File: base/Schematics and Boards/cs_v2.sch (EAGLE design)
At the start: 22 parts, among them U1 ATSAMD51, Y1 TSX-3225_16.0000MF09Z-AC3

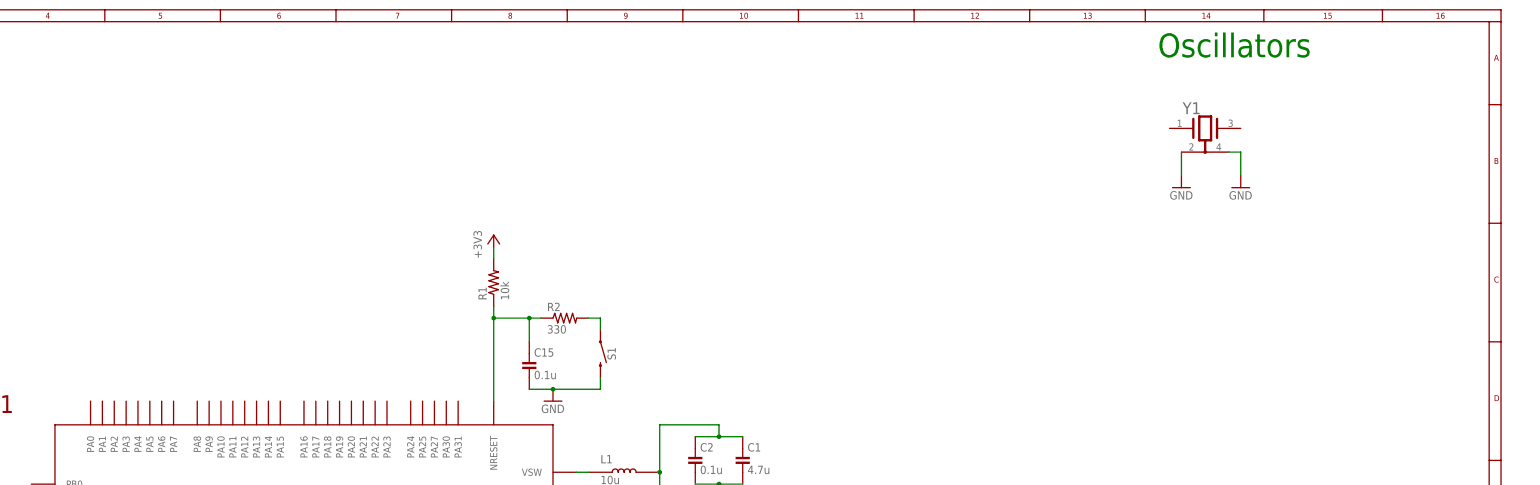
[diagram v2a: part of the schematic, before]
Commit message: Add crystals with loads and part numbers
16 MHz fast osc and 32.768 slow.
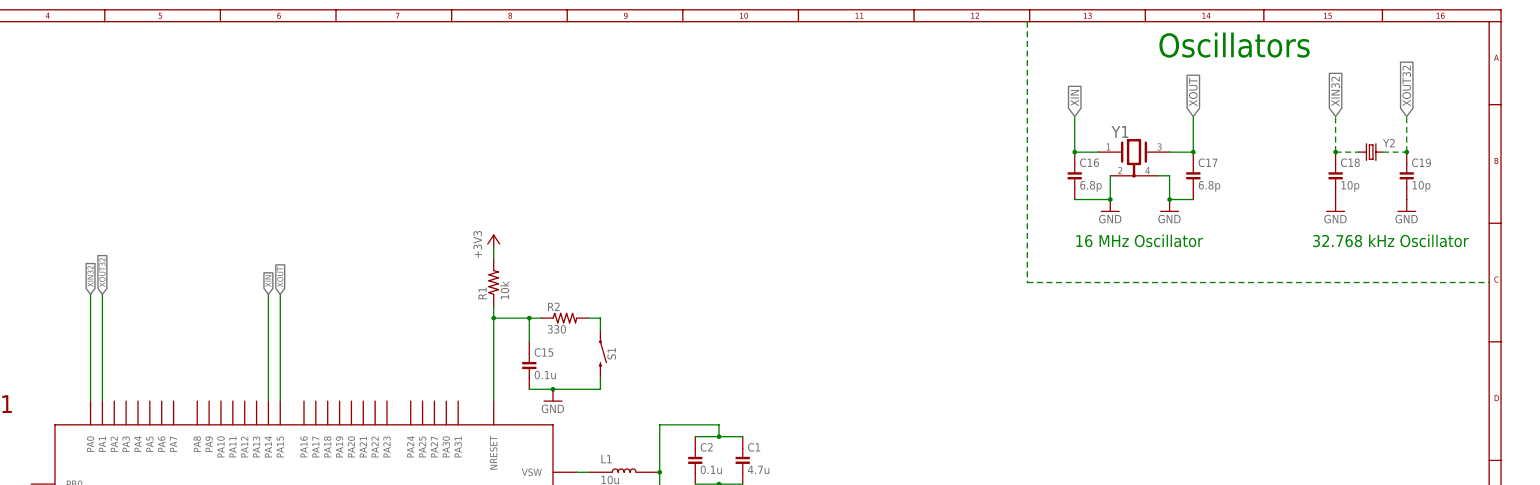
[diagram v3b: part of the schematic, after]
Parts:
- added C16, C17: 6.8p, Capacitors:C-0402
- added C18, C19: 10p, Capacitors:C-0402
- added Y2: ABRACON_ABS07-32.768KHZ-9-TABRACON_ABS07-32.768KHZ-7-T_0_0, Oscillators:ABRACON_ABS07-32.768KHZ-9-TABRACON_ABS07-32.768KHZ-7-T_0_0
- Y1: value TSX-3225_16.0000MF09Z-AC3 -> 16M
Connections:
- new net XIN: C16.1, U1.PA14, Y1.1
- new net XIN32: C18.1, U1.PA0, Y2.1
- new net XOUT: C17.1, U1.PA15, Y1.3
- new net XOUT32: C19.1, U1.PA1, Y2.2
- net GND: now also C16.2, C17.2, C18.2, C19.2
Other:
- note added: "16 MHz Oscillator"
- note added: "32.768 kHz Oscillator"
- moved on the sheet: Y1
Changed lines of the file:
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@@
 </part>
 <part name="S1" library="SparkFun-Switches" deviceset="MOMENTARY-SWITCH-SPST" device="-SMD-4.6X2.8MM"/>
-<part name="Y1" library="Oscillators" deviceset="TSX-3225_16.0000MF09Z-AC3" device=""/>
+<part name="Y1" library="Oscillators" deviceset="TSX-3225_16.0000MF09Z-AC3" device="" value="16M"/>
 <part name="GND6" library="Supplies" deviceset="GND" device=""/>
 <part name="GND8" library="Supplies" deviceset="GND" device=""/>
+<part name="C16" library="Capacitors" deviceset="C-" device="0402" value="6.8p">
+<attribute name="PART_NO" value="C0402C689D8GAC7867"/>
+</part>
+<part name="C17" library="Capacitors" deviceset="C-" device="0402" value="6.8p">
+<attribute name="PART_NO" value="C0402C689D8GAC7867"/>
+</part>
+<part name="Y2" library="Oscillators" deviceset="ABRACON_ABS07-32.768KHZ-9-T" device="ABRACON_ABS07-32.768KHZ-7-T_0_0"/>
+<part name="C18" library="Capacitors" deviceset="C-" device="0402" value="10p">
+<attribute name="PART_NO" value="C0402C100C8GACTU"/>
+</part>
+<part name="C19" library="Capacitors" deviceset="C-" device="0402" value="10p">
+<attribute name="PART_NO" value="C0402C100C8GACTU"/>
+</part>
+<part name="GND9" library="Supplies" deviceset="GND" device=""/>
+<part name="GND10" library="Supplies" deviceset="GND" device=""/>
 </parts>
 <sheets>
@@
 <text x="228.6" y="162.56" size="1.778" layer="91">Sch Checklist fig 59-1</text>
 <text x="325.12" y="264.16" size="5.08" layer="91">Oscillators</text>
+<text x="307.34" y="223.52" size="2.54" layer="91">16 MHz Oscillator</text>
+<text x="358.14" y="223.52" size="2.54" layer="91">32.768 kHz Oscillator</text>
 </plain>
 <instances>
@@
 <attribute name="NAME" x="207.264" y="200.66" size="1.778" layer="95" font="vector" rot="R270" align="bottom-center"/>
 </instance>
-<instance part="Y1" gate="A" x="330.2" y="256.54" smashed="yes">
-<attribute name="NAME" x="330.454" y="254.508" size="2.54" layer="95" align="top-left"/>
-</instance>
-<instance part="GND6" gate="1" x="330.2" y="236.22" smashed="yes">
-<attribute name="VALUE" x="327.66" y="233.68" size="1.778" layer="96"/>
-</instance>
-<instance part="GND8" gate="1" x="342.9" y="236.22" smashed="yes">
-<attribute name="VALUE" x="340.36" y="233.68" size="1.778" layer="96"/>
+<instance part="Y1" gate="A" x="314.96" y="251.46" smashed="yes">
+<attribute name="NAME" x="315.214" y="249.428" size="2.54" layer="95" align="top-left"/>
+</instance>
+<instance part="GND6" gate="1" x="314.96" y="231.14" smashed="yes">
+<attribute name="VALUE" x="312.42" y="228.6" size="1.778" layer="96"/>
+</instance>
+<instance part="GND8" gate="1" x="327.66" y="231.14" smashed="yes">
+<attribute name="VALUE" x="325.12" y="228.6" size="1.778" layer="96"/>
+</instance>
+<instance part="C16" gate="G$1" x="307.34" y="238.76" smashed="yes">
+<attribute name="NAME" x="308.356" y="240.665" size="1.778" layer="95"/>
+<attribute name="VALUE" x="308.356" y="235.839" size="1.778" layer="96"/>
+<attribute name="PART_NO" x="307.34" y="238.76" size="2.54" layer="96" display="off"/>
+</instance>
+<instance part="C17" gate="G$1" x="332.74" y="238.76" smashed="yes">
+<attribute name="NAME" x="333.756" y="240.665" size="1.778" layer="95"/>
+<attribute name="VALUE" x="333.756" y="235.839" size="1.778" layer="96"/>
+<attribute name="PART_NO" x="332.74" y="238.76" size="2.54" layer="96" display="off"/>
+</instance>
+<instance part="Y2" gate="G$1" x="370.84" y="243.84" smashed="yes">
+<attribute name="NAME" x="373.38" y="244.856" size="1.778" layer="95"/>
+</instance>
+<instance part="C18" gate="G$1" x="363.22" y="238.76" smashed="yes">
+<attribute name="NAME" x="364.236" y="240.665" size="1.778" layer="95"/>
+<attribute name="VALUE" x="364.236" y="235.839" size="1.778" layer="96"/>
+<attribute name="PART_NO" x="363.22" y="238.76" size="2.54" layer="96" display="off"/>
+</instance>
+<instance part="C19" gate="G$1" x="378.46" y="238.76" smashed="yes">
+<attribute name="NAME" x="379.476" y="240.665" size="1.778" layer="95"/>
+<attribute name="VALUE" x="379.476" y="235.839" size="1.778" layer="96"/>
+<attribute name="PART_NO" x="378.46" y="238.76" size="2.54" layer="96" display="off"/>
+</instance>
+<instance part="GND9" gate="1" x="363.22" y="231.14" smashed="yes">
+<attribute name="VALUE" x="360.68" y="228.6" size="1.778" layer="96"/>
+</instance>
+<instance part="GND10" gate="1" x="378.46" y="231.14" smashed="yes">
+<attribute name="VALUE" x="375.92" y="228.6" size="1.778" layer="96"/>
 </instance>
 </instances>
@@
 <segment>
 <pinref part="GND6" gate="1" pin="GND"/>
-<wire x1="330.2" y1="238.76" x2="330.2" y2="243.84" width="0.1524" layer="91"/>
+<wire x1="314.96" y1="233.68" x2="314.96" y2="238.76" width="0.1524" layer="91"/>
 <pinref part="Y1" gate="A" pin="1_GND"/>
+<pinref part="C16" gate="G$1" pin="2"/>
+<wire x1="307.34" y1="233.68" x2="314.96" y2="233.68" width="0.1524" layer="91"/>
+<junction x="314.96" y="233.68"/>
 </segment>
 <segment>
 <pinref part="GND8" gate="1" pin="GND"/>
 <pinref part="Y1" gate="A" pin="2_GND"/>
-<wire x1="342.9" y1="238.76" x2="342.9" y2="243.84" width="0.1524" layer="91"/>
-<wire x1="342.9" y1="243.84" x2="340.36" y2="243.84" width="0.1524" layer="91"/>
+<wire x1="327.66" y1="233.68" x2="327.66" y2="238.76" width="0.1524" layer="91"/>
+<wire x1="327.66" y1="238.76" x2="325.12" y2="238.76" width="0.1524" layer="91"/>
+<pinref part="C17" gate="G$1" pin="2"/>
+<wire x1="327.66" y1="233.68" x2="332.74" y2="233.68" width="0.1524" layer="91"/>
+<junction x="327.66" y="233.68"/>
+</segment>
+<segment>
+<pinref part="C18" gate="G$1" pin="2"/>
+<pinref part="GND9" gate="1" pin="GND"/>
+</segment>
+<segment>
+<pinref part="C19" gate="G$1" pin="2"/>
+<pinref part="GND10" gate="1" pin="GND"/>
 </segment>
 </net>
@@
 </segment>
 </net>
+<net name="XOUT" class="0">
+<segment>
+<pinref part="C17" gate="G$1" pin="1"/>
+<pinref part="Y1" gate="A" pin="3"/>
+<wire x1="332.74" y1="243.84" x2="327.66" y2="243.84" width="0.1524" layer="91"/>
+<wire x1="332.74" y1="243.84" x2="332.74" y2="251.46" width="0.1524" layer="91"/>
+<junction x="332.74" y="243.84"/>
+<label x="332.74" y="251.46" size="1.778" layer="95" rot="R90" xref="yes"/>
+</segment>
+<segment>
+<pinref part="U1" gate="G$1" pin="PA15"/>
+<wire x1="137.16" y1="190.5" x2="137.16" y2="213.36" width="0.1524" layer="91"/>
+<label x="137.16" y="213.36" size="1.27" layer="95" rot="R90" xref="yes"/>
+</segment>
+</net>
+<net name="XIN" class="0">
+<segment>
+<pinref part="C16" gate="G$1" pin="1"/>
+<pinref part="Y1" gate="A" pin="1"/>
+<wire x1="307.34" y1="243.84" x2="312.42" y2="243.84" width="0.1524" layer="91"/>
+<wire x1="307.34" y1="243.84" x2="307.34" y2="251.46" width="0.1524" layer="91"/>
+<junction x="307.34" y="243.84"/>
+<label x="307.34" y="251.46" size="1.778" layer="95" rot="R90" xref="yes"/>
+</segment>
+<segment>
+<pinref part="U1" gate="G$1" pin="PA14"/>
+<wire x1="134.62" y1="190.5" x2="134.62" y2="213.36" width="0.1524" layer="91"/>
+<label x="134.62" y="213.36" size="1.27" layer="95" rot="R90" xref="yes"/>
+</segment>
+</net>
+<net name="N$4" class="0">
+<segment>
+<wire x1="297.18" y1="271.78" x2="297.18" y2="215.9" width="0.254" layer="91" style="shortdash"/>
+<wire x1="297.18" y1="215.9" x2="396.24" y2="215.9" width="0.254" layer="91" style="shortdash"/>
+</segment>
+</net>
+<net name="XIN32" class="0">
+<segment>
+<pinref part="C18" gate="G$1" pin="1"/>
+<pinref part="Y2" gate="G$1" pin="1"/>
+<wire x1="363.22" y1="243.84" x2="368.3" y2="243.84" width="0.1524" layer="91" style="longdash"/>
+<wire x1="363.22" y1="243.84" x2="363.22" y2="251.46" width="0.1524" layer="91" style="longdash"/>
+<junction x="363.22" y="243.84"/>
+<label x="363.22" y="251.46" size="1.778" layer="95" rot="R90" xref="yes"/>
+</segment>
+<segment>
+<pinref part="U1" gate="G$1" pin="PA0"/>
+<wire x1="96.52" y1="213.36" x2="96.52" y2="190.5" width="0.1524" layer="91"/>
+<label x="96.52" y="213.36" size="1.27" layer="95" rot="R90" xref="yes"/>
+</segment>
+</net>
+<net name="XOUT32" class="0">
+<segment>
+<pinref part="Y2" gate="G$1" pin="2"/>
+<pinref part="C19" gate="G$1" pin="1"/>
+<wire x1="373.38" y1="243.84" x2="378.46" y2="243.84" width="0.1524" layer="91" style="longdash"/>
+<wire x1="378.46" y1="243.84" x2="378.46" y2="251.46" width="0.1524" layer="91" style="longdash"/>
+<junction x="378.46" y="243.84"/>
+<label x="378.46" y="251.46" size="1.778" layer="95" rot="R90" xref="yes"/>
+</segment>
+<segment>
+<pinref part="U1" gate="G$1" pin="PA1"/>
+<wire x1="99.06" y1="190.5" x2="99.06" y2="213.36" width="0.1524" layer="91"/>
+<label x="99.06" y="213.36" size="1.27" layer="95" rot="R90" xref="yes"/>
+</segment>
+</net>

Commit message: Add SD card parts, start on power subsystem
SD card parts added, but not connected to processor. Began on power subsystem. Decided to go with buck boost convertor from maxim. A few TI parts seemed like decent alternatives because they actually post their low-current efficiencies. Would be smart to inquire with maxim.
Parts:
- added C202: 100n, Capacitors:C-0402
- added C206: 470n, Capacitors:C-0402
- added J1: DM3AT-SF-PEJM5, DM3AT-SF-PEJM5:DM3AT-SF-PEJM5
- added J2: (no value), Connectors:J-JST2-SMT_RA-SH
- added R_SDCMD: 10K, Resistors:R-0402
- added R_SD_DET1: 510k, Resistors:R-0402
- added S2: (no value), Switches:SLIDESWITCH-SPDT-SMD-RIGHT-ANGLE
- added U2: MAX77827BEWC+T, Regulators:MAX77827BEWC+T
- added U202: COULOMB-MAX17262, CoulombCounters:COULOMB-MAX17262
- Y1: device Oscillators:TSX-3225_16.0000MF09Z-AC3 -> Oscillators:EPSON_TSX-3225_16.0000MF09Z-AC3
- Y2: value ABRACON_ABS07-32.768KHZ-9-TABRACON_ABS07-32.768KHZ-7-T_0_0 -> ABS07-32.768KHZ-9-T; device Oscillators:ABRACON_ABS07-32.768KHZ-9-TABRACON_ABS07-32.768KHZ-7-T_0_0 -> Oscillators:ABS07-32.768KHZ-9-T
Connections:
- net +3V3 renamed +3V3_PROC
- removed net GND1: C11.2, C12.2, C13.2
- new net +3V3_SD: J1.VDD, R_SDCMD.2, R_SD_DET1.1
- new net +3V7_BATT: U202.SYS
- new net +3V7_BATT_IN: C202.1, S2.S, U202.BATT, U202.TH
- new net ADDR_I2C_CLK: U202.SCL
- new net ADDR_I2C_DAT: U202.SDA
- new net BATT_ALERT: U202.ALRT
- new net N$13: C206.1, U202.REG
- new net N$7: J2.1, S2.P
- new net N$8: S2.O
- new net SDIO_CLK: J1.CLK
- new net SDIO_CMD: J1.CMD, R_SDCMD.1
- new net SDIO_D0: J1.DAT0
- new net SDIO_D1: J1.DAT1
- new net SDIO_D2: J1.DAT2
- new net SDIO_D3: J1.CD/DAT3
- new net SD_DETECT: J1.A, R_SD_DET1.2
- net GND: now also C11.2, C12.2, C13.2, C202.2, C206.2, J1.B, J1.SHIELD, J1.VSS, J2.2, U202.GND
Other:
- note added: "3V7 BATT needs to be included in the debug header so that it can charge the battery from there; no charger on this board"
- note added: "Double check polarity!!"
- note added: "Using SH type connector (1mm pitch), as opposed to PH type (2mm pitch). Height chopped in half, but carries less current (1A rating) and is more prone to rip off. Unlikely to find many batteries with this connector by default."
- note removed: "Separate analog GND?"

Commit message: Add load switch, sense resistors, breakout headers, and comments
Load switch for SD card.

Sense resistors daughter card header, processor, and SD card.

Added 80 and 30 pin receptacles to design for daughter and debug cards, respectively. Pin count is a guess for now.

Comments for power subsystem. In particular, comments on sense resistors and charging circuit (residing on debug card).
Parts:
- added C20: 0.1u, Capacitors:C-0402
- added C21: 1u, Capacitors:C-0603
- added C_REG_BIAS: 1u, Capacitors:C-0402
- added C_REG_IN: 10u, Capacitors:C-0603
- added C_REG_OUT: 22u, Capacitors:C-0805
- added J_DBG: HIROSE_DF40_30-PIN_CONNECTORS, Connectors:HIROSE_DF40_30-PIN_CONNECTORS
- added J_DTR: HIROSE-DF40_80-PIN_CONNECTORS, Connectors:HIROSE-DF40_80-PIN_CONNECTORS
- added L3: 1u, Inductors:L1008
- added R3: 0, Resistors:R-2010
- added R_SENSE_DTR: 0.5, Resistors:R-0603
- added R_SENSE_PROC, R_SENSE_SD: 1, Resistors:R-0603
- added U206: LOADSWITCH-MIC94162, Switches:LOADSWITCH-MIC94162
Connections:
- new net +3V3: C_REG_OUT.1, R_SENSE_DTR.1, R_SENSE_PROC.1, R_SENSE_SD.1, U2.OUT, U2.OUTS
- new net +3V3_DTR: R_SENSE_DTR.2
- new net +3V3_SD_SENSE: C21.1, R_SENSE_SD.2, U206.VIN
- new net AGND: C_REG_BIAS.2, R3.1, U2.AGND
- new net EN_SD: U206.ENABLE
- new net N$10: L3.2, U2.LX2
- new net N$11: C_REG_BIAS.1, U2.BIAS
- new net N$9: L3.1, U2.LX1
- net +3V3_PROC: now also R_SENSE_PROC.2
- net +3V3_SD: now also C20.1, U206.VOUT
- net +3V7_BATT: now also C_REG_IN.1, U2.EN, U2.IN
- net GND: now also C20.2, C21.2, C_REG_IN.2, C_REG_OUT.2, R3.2, U2.FPWM, U2.PGND, U206.GND
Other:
- note added: "Need p-channel mosfet here to select between battery input and the charger output from debug. Switch enabled by that votlage from charger"
- note added: "POK is open drain output. Unused, so left floating. SEL left open for 3V3 output. Both SEL and POK are center pins in WLP, so simplest to leave unused or tied to GND"
- note added: "Pinout Headers"
- note added: "Power"
- note added: "Processor"
- note added: "Route analog signals through this resistor. The resistor is big and fat for this purpose!"
- note added: "Sense resistor values are suggetions. These values may need to be updated. They should, for max current draw, have no more than 100 mV drop on 3.3V output."
- note added: "Sense resistors exist for high side current monitors. Another processor/ADC on the debug board should calculate the differential voltage across the resistor, and use this to determine power input to the load at high resolution. Differential voltage should be at most 100 mV, so an amplifier should scale up that differential voltage"

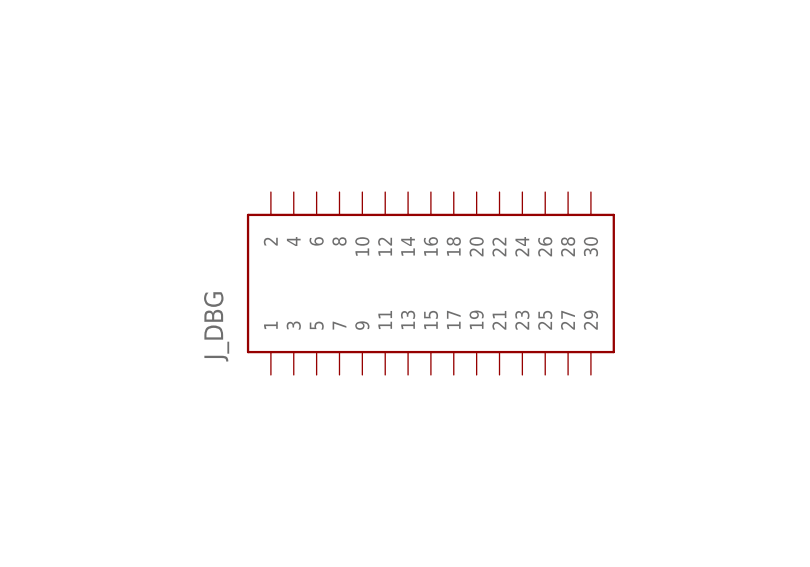
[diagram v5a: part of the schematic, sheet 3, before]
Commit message: Remove 30-pin header temporarily -- bad footprint
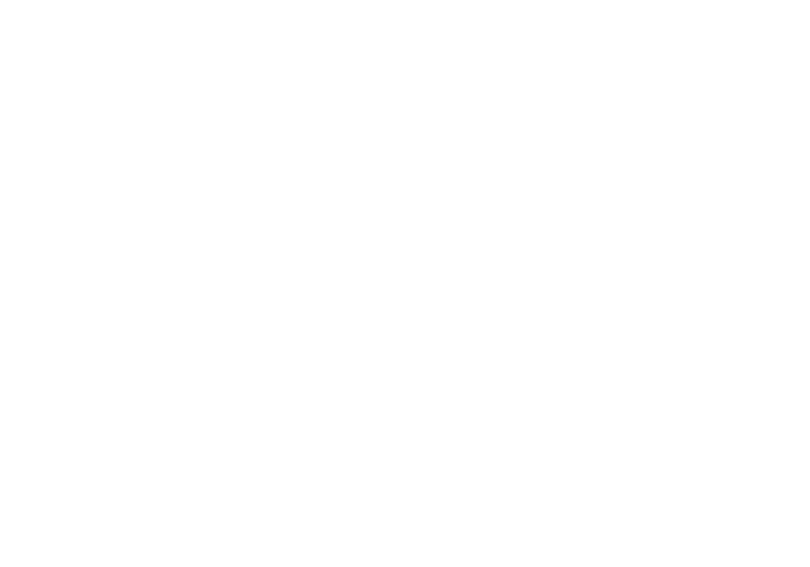
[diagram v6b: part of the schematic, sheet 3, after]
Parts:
- removed J_DBG: HIROSE_DF40_30-PIN_CONNECTORS, Connectors:HIROSE_DF40_30-PIN_CONNECTORS
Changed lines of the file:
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@@
 </part>
 <part name="BORDER4" library="Graphics" deviceset="BORDER-CMU" device=""/>
-<part name="J_DBG" library="Connectors" deviceset="HIROSE_DF40_30-PIN_CONNECTORS" device=""/>
 <part name="J_DTR" library="Connectors" deviceset="HIROSE-DF40_80-PIN_CONNECTORS" device=""/>
 </parts>
@@
 <attribute name="SHEET" x="337.82" y="4.2672" size="1.778" layer="94"/>
 </instance>
-<instance part="J_DBG" gate="A" x="294.64" y="137.16" smashed="yes" rot="R90">
-<attribute name="NAME" x="289.3314" y="141.3256" size="2.0828" layer="95" ratio="6" rot="SR90"/>
-</instance>
 <instance part="J_DTR" gate="G$1" x="132.08" y="149.86" smashed="yes" rot="R90">

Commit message: Add power source selection; clean up pwr subsystem
Battery charger will not be on main board, so power source selection hardware needs to be here to provide regulator with correct input. Using p-channel mosfet and schottky diode w/ low reverse current for expected voltages. This design was based on Adafruit boards, but exact parts were carefully selected.
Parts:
- added Q1: DMG3415UFY4Q-7, Diodes:P-CH_MOSFET_DMG3415UFY4Q-7
- added R4: 100k, Resistors:R-0402
- added U3: PD3S140-7, Diodes:PD3S140-7
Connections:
- net N$10 renamed VREG_LX2
- net N$11 renamed VREG_BIAS
- net N$9 renamed VREG_LX1
- new net VDD_DBG: Q1.G, R4.2, U3.P
- new net VREG_IN: C_REG_IN.1, Q1.S, U2.EN, U2.IN, U3.N
- net +3V7_BATT: now also Q1.D; no longer C_REG_IN.1, U2.EN, U2.IN
- net GND: now also R4.1
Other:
- note added: "3.3 V Regulator"
- note added: "Battery and Coulomb Counter"
- note added: "Buck-boost convertor"
- note added: "Ground Connection"
- note added: "Load Switches & Sense Resistors"
- note added: "P-channel MOSFET to select regulator input between battery and debug power rail. Schottky diode w/ low reverse bias current to isolate debug power rail from vreg in when not connected"
- note added: "Power Source Selection"
- note added: "VDD_DBG comes from debug/aux power board. Should be an alternative power source like solar or USB. If charger is on that board, then VDD_DBG should be charger output"
- note removed: "Need p-channel mosfet here to select between battery input and the charger output from debug. Switch enabled by that votlage from charger"
- moved on the sheet: C20, C202, C206, C21, C_REG_BIAS, C_REG_IN, C_REG_OUT, J2, L3, R3, R_SENSE_DTR, R_SENSE_PROC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
